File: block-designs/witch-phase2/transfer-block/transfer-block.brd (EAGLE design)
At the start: 27.9 x 27.9 mm, 15 parts, among them IC1 74LVC1G18DBVR, IC2 74AHC1G00DBV, IC3 741G3157DBVR, IC4 741G175, IC5 741G3157DBVR

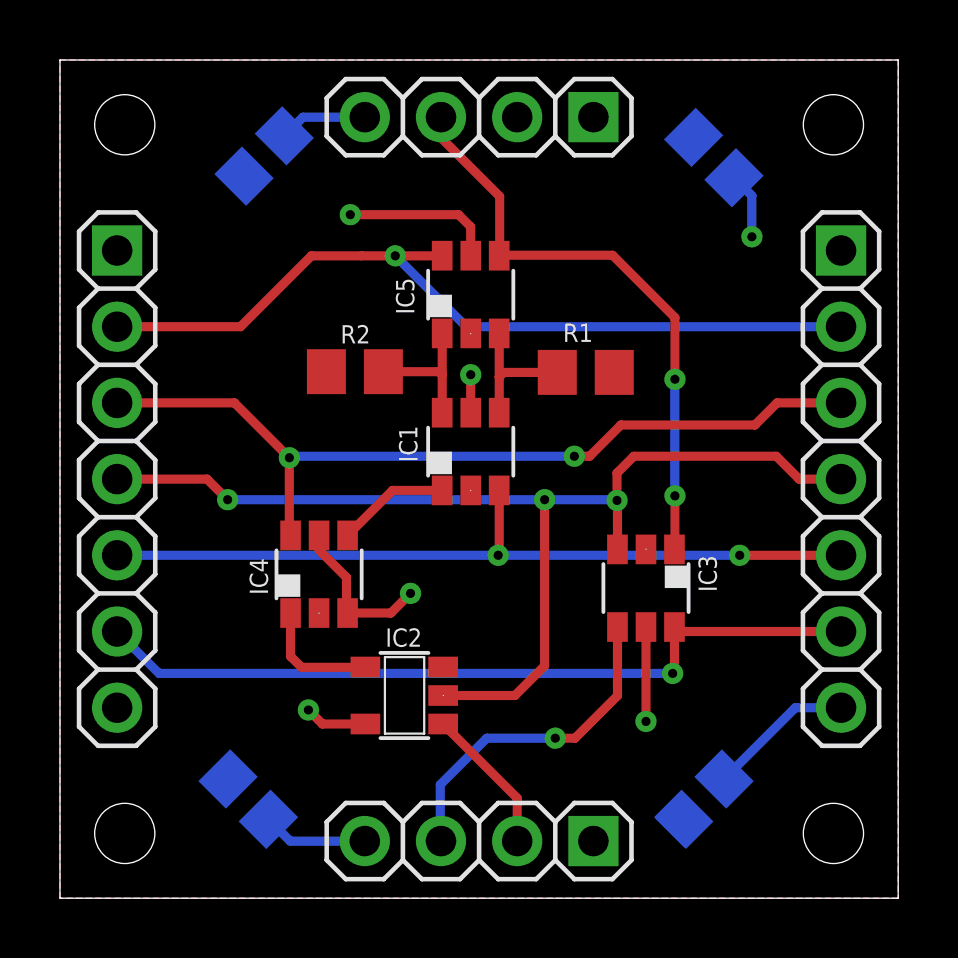
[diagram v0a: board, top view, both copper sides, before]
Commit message: adjust borders for ground/vcc plains and size to match 1.1inch grids
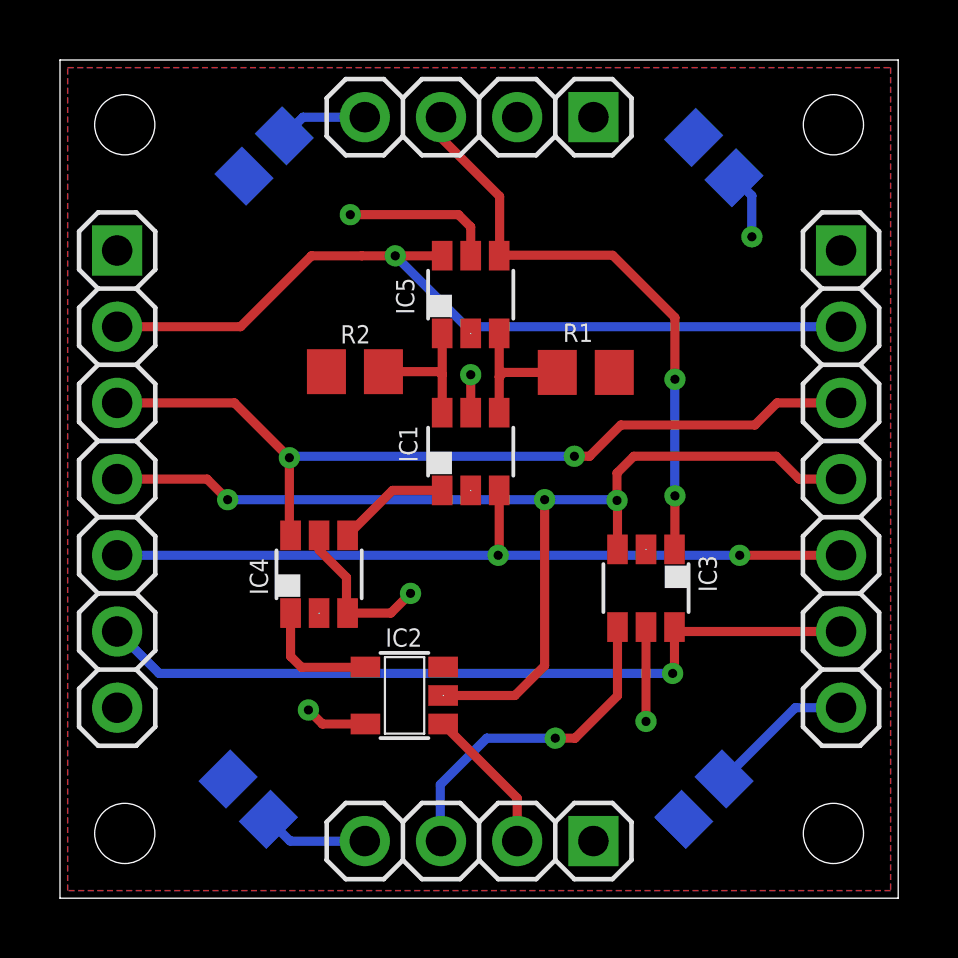
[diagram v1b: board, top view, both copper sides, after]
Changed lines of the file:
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@@
 <contactref element="JP1" pad="4"/>
 <contactref element="JP3" pad="4"/>
-<polygon width="0" layer="1">
-<vertex x="27.94" y="0"/>
-<vertex x="0" y="0"/>
-<vertex x="0" y="27.94"/>
-<vertex x="27.94" y="27.94"/>
+<polygon width="0.254" layer="1">
+<vertex x="27.686" y="0.254"/>
+<vertex x="0.254" y="0.254"/>
+<vertex x="0.254" y="27.686"/>
+<vertex x="27.686" y="27.686"/>
 </polygon>
 <contactref element="IC1" pad="2"/>
@@
 <contactref element="JP3" pad="1"/>
 <contactref element="IC2" pad="5"/>
-<polygon width="0" layer="16">
-<vertex x="27.94" y="0"/>
-<vertex x="0" y="0"/>
-<vertex x="0" y="27.94"/>
-<vertex x="27.94" y="27.94"/>
+<polygon width="0.254" layer="16">
+<vertex x="27.686" y="0.254"/>
+<vertex x="0.254" y="0.254"/>
+<vertex x="0.254" y="27.686"/>
+<vertex x="27.686" y="27.686"/>
 </polygon>
 <contactref element="JP4" pad="1"/>

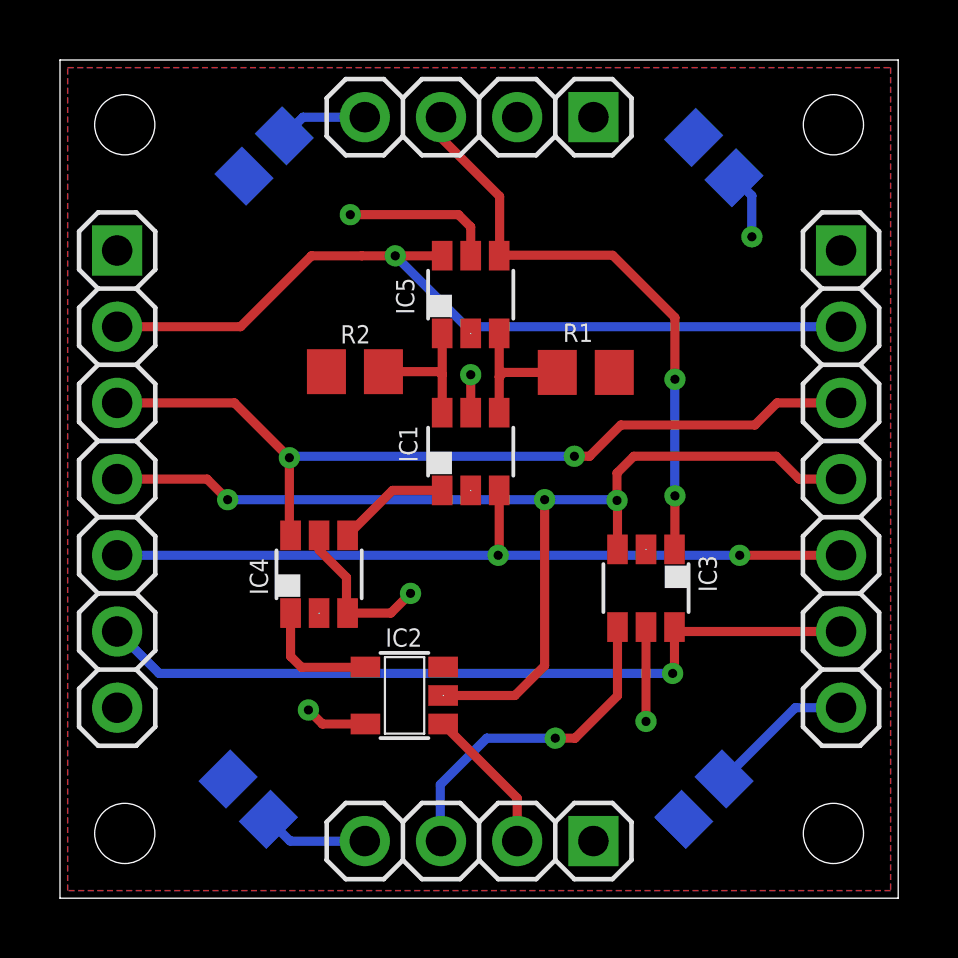
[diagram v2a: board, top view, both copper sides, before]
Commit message: updated designs for new labeling and spacing
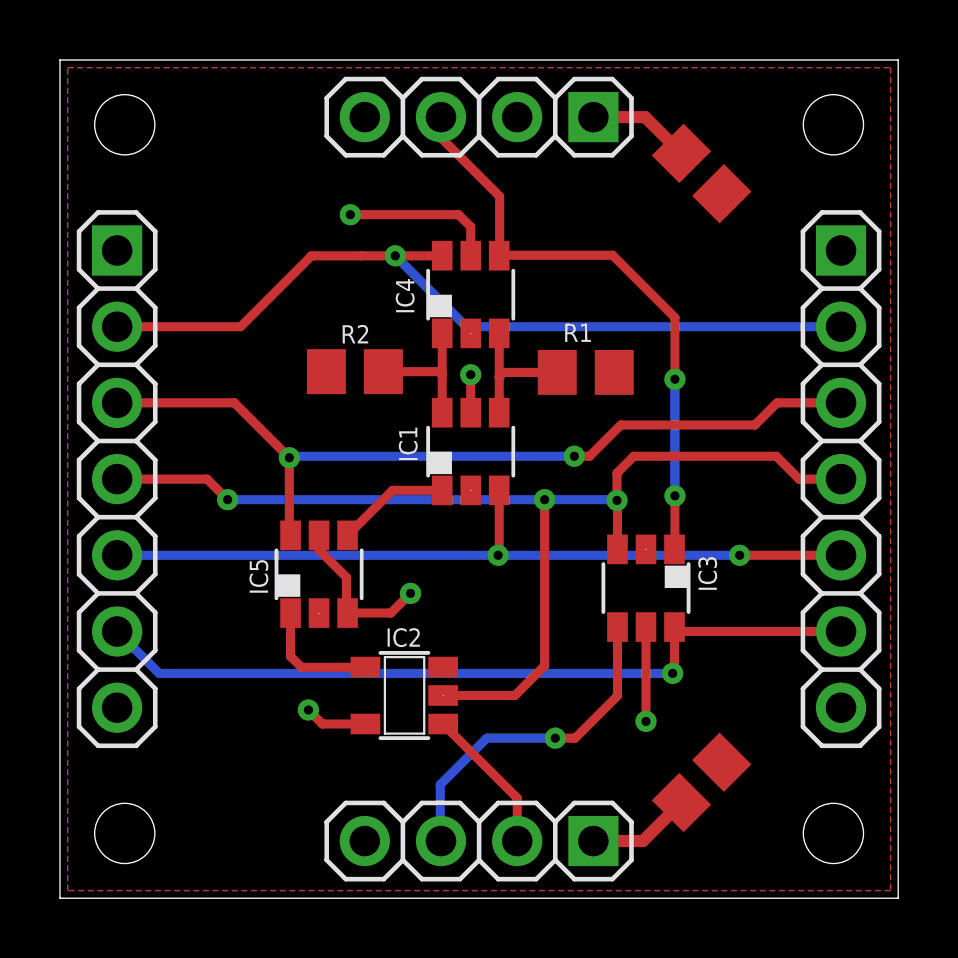
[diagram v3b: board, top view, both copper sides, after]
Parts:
- removed C3, C4: (no value), resistor:C0805
- IC4: value 741G175 -> 741G3157DBVR
- IC5: value 741G3157DBVR -> 741G175
- moved C2 14.6 mm to (21.4, 24.2), flipped to the top, turned to 315 degrees
- moved IC4 10.6 mm to (13.7, 20.1)
- moved IC5 10.6 mm to (8.64, 10.8)
- moved C1 0.56 mm to (21.4, 3.86), flipped to the top, turned to 45 degrees
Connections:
- net ADD/COMP: now also IC4.6; no longer IC5.6
- net GND: no longer C3.2, C4.2
- net N$4: now also IC4.3; no longer IC5.3
- net N$5: now also IC4.1; no longer IC5.1
- net RCV_CLK: now also IC4.4; no longer IC5.4
- net RESET: now also IC5.6; no longer IC4.6
- net SELECT: now also IC5.4; no longer IC4.4
- net VCC: now also IC5.3; no longer C3.1, C4.1, IC4.3
- net ZC_EN: now also IC5.1; no longer IC4.1
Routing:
- net GND: track 13.6 -> 0.00 mm, vias 1 -> 0
- net VCC: track 17.0 -> 23.9 mm
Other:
- board text added: "XFER UNIT"
- board text removed: "TOP"
- board text removed: "TRANSFER UNIT"
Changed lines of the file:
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@@
 <circle x="2.159" y="2.159" radius="2.0066" width="0.0254" layer="41"/>
 <circle x="2.159" y="2.159" radius="2.0066" width="0.0254" layer="42"/>
-<text x="5.7912" y="25.4508" size="1.016" layer="48">TOP</text>
-<text x="4.5466" y="2.6162" size="0.6096" layer="48">TRANSFER
+<text x="8.636" y="3.4798" size="1.1176" layer="48" rot="R135">XFER
 UNIT</text>
 </plain>
@@
 </autorouter>
 <elements>
-<element name="C1" library="resistor" package="C0805" value="" x="21.463" y="3.302" smashed="yes" rot="MR135">
-<attribute name="NAME" x="20.115959375" y="1.09285625" size="0.6096" layer="26" rot="MR45"/>
-<attribute name="VALUE" x="19.217940625" y="4.289828125" size="1.27" layer="28" rot="MR135"/>
-</element>
-<element name="C2" library="resistor" package="C0805" value="" x="6.8072" y="24.7396" smashed="yes" rot="MR135">
-<attribute name="NAME" x="7.15835" y="23.490421875" size="0.6096" layer="26" rot="MR135"/>
-<attribute name="VALUE" x="4.562134375" y="25.727428125" size="1.27" layer="28" rot="MR135"/>
-</element>
-<element name="C3" library="resistor" package="C0805" value="" x="6.2738" y="3.302" smashed="yes" rot="MR225">
-<attribute name="NAME" x="5.129959375" y="2.882" size="0.6096" layer="26" rot="MR225"/>
-<attribute name="VALUE" x="7.261628125" y="5.547065625" size="1.27" layer="28" rot="MR225"/>
-</element>
-<element name="C4" library="resistor" package="C0805" value="" x="21.7932" y="24.6888" smashed="yes" rot="MR225">
-<attribute name="NAME" x="22.7321625" y="26.173796875" size="0.6096" layer="26" rot="MR225"/>
-<attribute name="VALUE" x="22.78103125" y="26.9338625" size="1.27" layer="28" rot="MR225"/>
+<element name="C1" library="resistor" package="C0805" value="" x="21.3868" y="3.8608" smashed="yes" rot="R45">
+<attribute name="VALUE" x="22.374628125" y="1.615740625" size="1.27" layer="27" rot="R45"/>
+</element>
+<element name="C2" library="resistor" package="C0805" value="" x="21.3868" y="24.1554" smashed="yes" rot="R315">
+<attribute name="VALUE" x="19.1417375" y="23.16756875" size="1.27" layer="27" rot="R315"/>
 </element>
 <element name="JP1" library="pinhead" package="1X04" value="" x="13.97" y="26.035" smashed="yes" rot="R180">
@@
 <attribute name="NAME" x="11.9126" y="14.5288" size="0.6096" layer="25" rot="R90"/>
 </element>
-<element name="IC5" library="74xx-little-us" package="DBV_R-PDSO-G6" value="741G3157DBVR" x="13.6906" y="20.1168" smashed="yes">
+<element name="IC4" library="74xx-little-us" package="DBV_R-PDSO-G6" value="741G3157DBVR" x="13.6906" y="20.1168" smashed="yes">
 <attribute name="NAME" x="11.811" y="19.4564" size="0.6096" layer="25" rot="R90"/>
 </element>
@@
 <attribute name="NAME" x="21.2852" y="11.43" size="0.6096" layer="25" rot="R270"/>
 </element>
-<element name="IC4" library="74xx-little-us" package="DBV_R-PDSO-G6" value="741G175" x="8.636" y="10.795" smashed="yes">
+<element name="IC5" library="74xx-little-us" package="DBV_R-PDSO-G6" value="741G175" x="8.636" y="10.795" smashed="yes">
 <attribute name="NAME" x="6.9342" y="10.1092" size="0.6096" layer="25" rot="R90"/>
 </element>
@@
 <signals>
 <signal name="GND">
-<contactref element="C3" pad="2"/>
 <contactref element="C1" pad="2"/>
 <contactref element="C2" pad="2"/>
-<contactref element="C4" pad="2"/>
 <contactref element="JP1" pad="4"/>
 <contactref element="JP3" pad="4"/>
@@
 </polygon>
 <contactref element="IC1" pad="2"/>
-<contactref element="IC5" pad="2"/>
+<contactref element="IC4" pad="2"/>
 <contactref element="R2" pad="2"/>
 <contactref element="R1" pad="2"/>
@@
 <contactref element="JP4" pad="7"/>
 <contactref element="IC3" pad="2"/>
-<contactref element="IC4" pad="2"/>
-<wire x1="26.035" y1="6.35" x2="24.511003125" y2="6.35" width="0.3048" layer="16"/>
-<wire x1="24.511003125" y1="6.35" x2="22.134753125" y2="3.97375" width="0.3048" layer="16"/>
-<wire x1="6.945553125" y1="2.630246875" x2="7.6708" y2="1.905" width="0.3048" layer="16"/>
-<wire x1="7.6708" y1="1.905" x2="10.16" y2="1.905" width="0.3048" layer="16"/>
-<via x="23.0632" y="22.0472" extent="1-16" drill="0.3048"/>
-<wire x1="22.464953125" y1="24.017046875" x2="23.0632" y2="23.4188" width="0.3048" layer="16"/>
-<wire x1="23.0632" y1="23.4188" x2="23.0632" y2="22.0472" width="0.3048" layer="16"/>
-<wire x1="7.478953125" y1="25.41135" x2="8.102603125" y2="26.035" width="0.3048" layer="16"/>
-<wire x1="8.102603125" y1="26.035" x2="10.16" y2="26.035" width="0.3048" layer="16"/>
+<contactref element="IC5" pad="2"/>
 </signal>
 <signal name="VCC">
 <contactref element="IC1" pad="5"/>
-<contactref element="IC5" pad="5"/>
+<contactref element="IC4" pad="5"/>
 <contactref element="C1" pad="1"/>
 <contactref element="C2" pad="1"/>
-<contactref element="C4" pad="1"/>
-<contactref element="C3" pad="1"/>
 <contactref element="JP1" pad="1"/>
 <contactref element="JP3" pad="1"/>
@@
 <contactref element="JP2" pad="1"/>
 <contactref element="IC3" pad="5"/>
-<contactref element="IC4" pad="5"/>
-<contactref element="IC4" pad="3"/>
+<contactref element="IC5" pad="5"/>
+<contactref element="IC5" pad="3"/>
 <wire x1="8.636" y1="12.095" x2="8.636" y2="11.6078" width="0.3048" layer="1"/>
 <wire x1="8.636" y1="11.6078" x2="9.5504" y2="10.6934" width="0.3048" layer="1"/>
@@
 <wire x1="13.6906" y1="22.3774" x2="13.2842" y2="22.7838" width="0.3048" layer="1"/>
 <wire x1="13.2842" y1="22.7838" x2="9.6774" y2="22.7838" width="0.3048" layer="1"/>
+<wire x1="17.78" y1="26.035" x2="19.507196875" y2="26.035" width="0.4064" layer="1"/>
+<wire x1="19.507196875" y1="26.035" x2="20.715046875" y2="24.82715" width="0.4064" layer="1"/>
+<wire x1="17.78" y1="1.905" x2="19.431" y2="1.905" width="0.4064" layer="1"/>
+<wire x1="19.431" y1="1.905" x2="20.715046875" y2="3.189046875" width="0.4064" layer="1"/>
 </signal>
 <signal name="N$4">
 <contactref element="IC1" pad="4"/>
-<contactref element="IC5" pad="3"/>
+<contactref element="IC4" pad="3"/>
 <contactref element="R1" pad="1"/>
 <wire x1="14.6406" y1="18.8268" x2="14.6406" y2="17.3736" width="0.3048" layer="1"/>
@@
 <signal name="N$5">
 <contactref element="IC1" pad="6"/>
-<contactref element="IC5" pad="1"/>
+<contactref element="IC4" pad="1"/>
 <contactref element="R2" pad="1"/>
 <wire x1="12.7406" y1="18.8268" x2="12.7406" y2="17.4498" width="0.3048" layer="1"/>
@@
 </signal>
 <signal name="ADD/COMP">
-<contactref element="IC5" pad="6"/>
+<contactref element="IC4" pad="6"/>
 <contactref element="JP4" pad="2"/>
 <contactref element="JP2" pad="2"/>
@@
 <signal name="SELECT">
 <contactref element="IC1" pad="1"/>
-<contactref element="IC4" pad="4"/>
+<contactref element="IC5" pad="4"/>
 <wire x1="12.7406" y1="13.5944" x2="11.0854" y2="13.5944" width="0.3048" layer="1"/>
 <wire x1="11.0854" y1="13.5944" x2="9.586" y2="12.095" width="0.3048" layer="1"/>
@@
 <signal name="ZC_EN">
 <contactref element="IC2" pad="4"/>
-<contactref element="IC4" pad="1"/>
+<contactref element="IC5" pad="1"/>
 <wire x1="7.686" y1="9.505" x2="7.686" y2="8.062" width="0.3048" layer="1"/>
 <wire x1="7.686" y1="8.062" x2="8.0518" y2="7.6962" width="0.3048" layer="1"/>
@@
 <signal name="RCV_CLK">
 <contactref element="JP1" pad="3"/>
-<contactref element="IC5" pad="4"/>
+<contactref element="IC4" pad="4"/>
 <contactref element="IC3" pad="1"/>
 <wire x1="12.7" y1="26.035" x2="12.7" y2="25.3492" width="0.3048" layer="1"/>
@@
 <contactref element="JP2" pad="3"/>
 <contactref element="JP4" pad="3"/>
-<contactref element="IC4" pad="6"/>
+<contactref element="IC5" pad="6"/>
 <wire x1="1.905" y1="16.51" x2="5.8166" y2="16.51" width="0.3048" layer="1"/>
 <wire x1="5.8166" y1="16.51" x2="7.6454" y2="14.6812" width="0.3048" layer="1"/>

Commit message: updated layout with additional caps and change to 0603 passive. changed clock input to use a 71LVC1G97 configured as AND gate with one input inverted
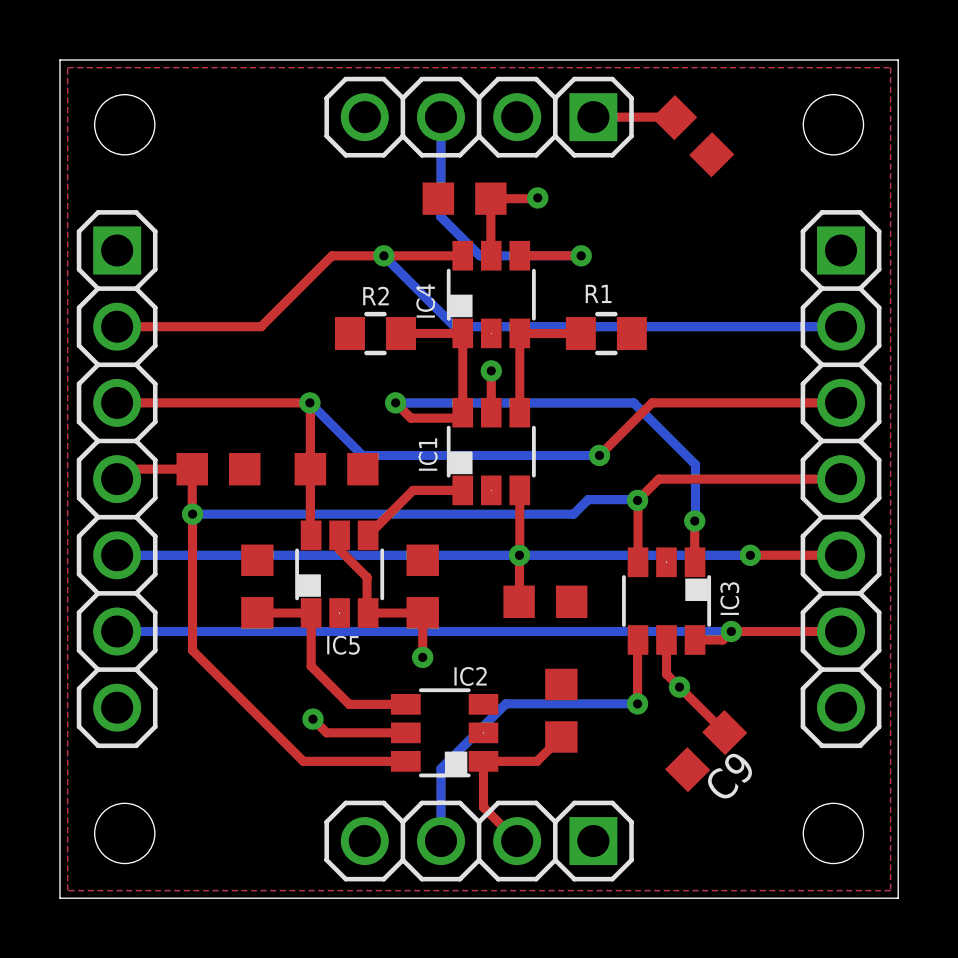
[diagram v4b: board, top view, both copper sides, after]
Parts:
- added C3, C4, C5, C6, C7, C8, C9: (no value), resistor:C0603K
- C1, C2: device resistor:C0805 -> resistor:C0603K
- IC1: value 74LVC1G18DBVR -> 741G18DBVR; device 74xx-little-us:DBV_R-PDSO-G6 -> witch-e:DBV_R-PDSO-G6
- IC2: value 74AHC1G00DBV -> 741G97DBVR; device 74xx-little-us:SOT23-5 -> witch-e:DBV_R-PDSO-G6
- IC3, IC4: value 741G3157DBVR -> 741G157DBVR
- IC5: value 741G175 -> 741G175DBVR; device 74xx-little-us:DBV_R-PDSO-G6 -> witch-e:DBV_R-PDSO-G6
- R1, R2: device resistor:R0805 -> resistor:R0603
- moved C1 21.5 mm to (21.1, 25.4), turned to 315 degrees
- moved C2 7.94 mm to (13.5, 23.3), turned to 180 degrees
- moved IC2 1.83 mm to (12.8, 5.51)
- moved R1 1.47 mm to (18.2, 18.8)
- moved R2 1.44 mm to (10.5, 18.8)
- moved IC3 0.81 mm to (20.2, 9.91)
- moved IC1 0.69 mm to (14.4, 14.9)
- moved IC4 0.69 mm to (14.4, 20.1)
- moved IC5 0.69 mm to (9.32, 10.8)
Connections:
- net N$4 renamed ADD
- removed net N$5: IC1.6, IC4.1, R2.1
- new net COMP: IC1.6, IC3.1, IC4.1, R2.1
- new net GND1: IC2.3
- net 10A_PULSE: now also C6.1, IC2.6; no longer IC2.2
- net 9A_PULSE: now also C7.1
- net GND: now also C3.2, C4.2, C5.2, C6.2, C7.2, C8.2, C9.2, IC2.2; no longer IC2.3
- net RCV_CLK: no longer IC3.1
- net RESET: now also C5.1
- net SND_ZC: now also C8.1
- net VCC: now also C4.1, C9.1
- net ZC_EN: now also C3.1
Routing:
- net COMP: track 0.00 -> 21.3 mm, vias 0 -> 2
- net RCV_CLK: track 19.9 -> 10.6 mm, vias 2 -> 1
- net 10A_PULSE: track 36.9 -> 41.5 mm, vias 3 -> 2
- net N$5: track 4.65 -> 0.00 mm
- net ZC_EN: track 4.09 -> 7.25 mm
- net VCC: track 23.9 -> 21.1 mm
- net RESET: track 28.2 -> 30.1 mm
- net 9A_PULSE: track 26.3 -> 27.9 mm
- net SND_ZC: track 4.92 -> 6.06 mm
- net ADD/COMP: track 27.7 -> 28.7 mm
- net CLR: track 26.4 -> 25.5 mm
- net SND_CLK: track 11.3 -> 12.0 mm
